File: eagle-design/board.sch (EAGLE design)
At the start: 13 parts, among them IC1 7805T

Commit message: Addedd new design
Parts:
- removed JP6: (no value), pinhead:PINHD-1X4
- added JP9: (no value), pinhead:PINHD-1X10
- added R2, R3, R4, R5, R6, R7, R8, R9: 10k, rcl:R-US_0207/10
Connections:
- new net N$13: B1.33, JP1.14
- new net N$14: B1.3, U$1.D0
- new net N$15: JP1.11, U$1.D2
- new net N$16: B1.29, JP1.12
- new net N$17: B1.31, JP1.13
- new net N$18: B1.35, JP1.15
- new net N$19: JP1.16, U$1.D1
- new net N$20: JP1.6, U$1.D6
- new net N$21: JP1.3, U$1.D8
- new net N$22: JP1.4, U$1.D5
- new net N$23: B1.53/!CS, JP1.7
- new net N$24: JP1.5, U$1.D7
- new net N$25: B1.52/SCK, JP1.8
- new net N$26: B1.51/MOSI, JP1.9
- new net N$27: B1.25, JP9.3, R2.2
- new net N$28: B1.50/MISO, JP1.10
- new net N$29: B1.27, JP9.4, R3.1
- new net N$30: B1.37, JP9.5, R4.1
- new net N$31: B1.39, JP9.6, R5.1
- new net N$32: B1.41, JP9.7, R6.1
- new net N$33: B1.43, JP9.8, R7.1
- new net N$34: B1.45, JP9.9, R8.1
- new net N$35: B1.47, JP9.10, R9.1
- new net N$9: B1.2, U$1.D4
- net N$11: no longer JP6.4
- net N$2: now also JP1.2
- net N$3: now also JP9.1, R2.1, R3.2, R4.2, R5.2, R6.2, R7.2, R8.2, R9.2; no longer JP6.1
- net N$4: now also JP1.1
- net N$5: now also B1.23
- net N$6: no longer JP6.3
- net N$7: now also JP9.2; no longer JP6.2
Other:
- moved on the sheet: IC1, J2, JP2, JP3, JP4, JP5, JP7, JP8, R1, U$1

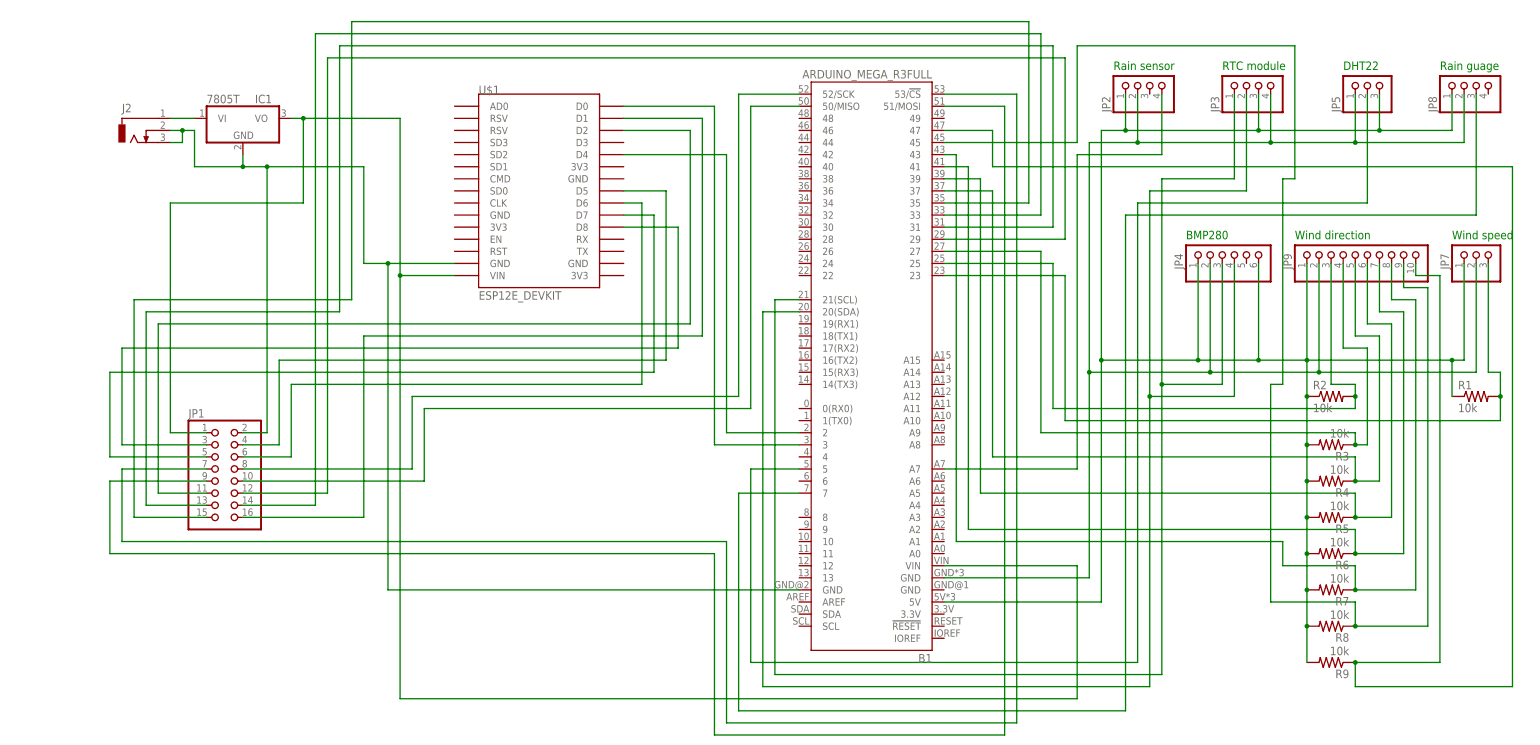
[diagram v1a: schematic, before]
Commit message: Added motherboard design and image exports
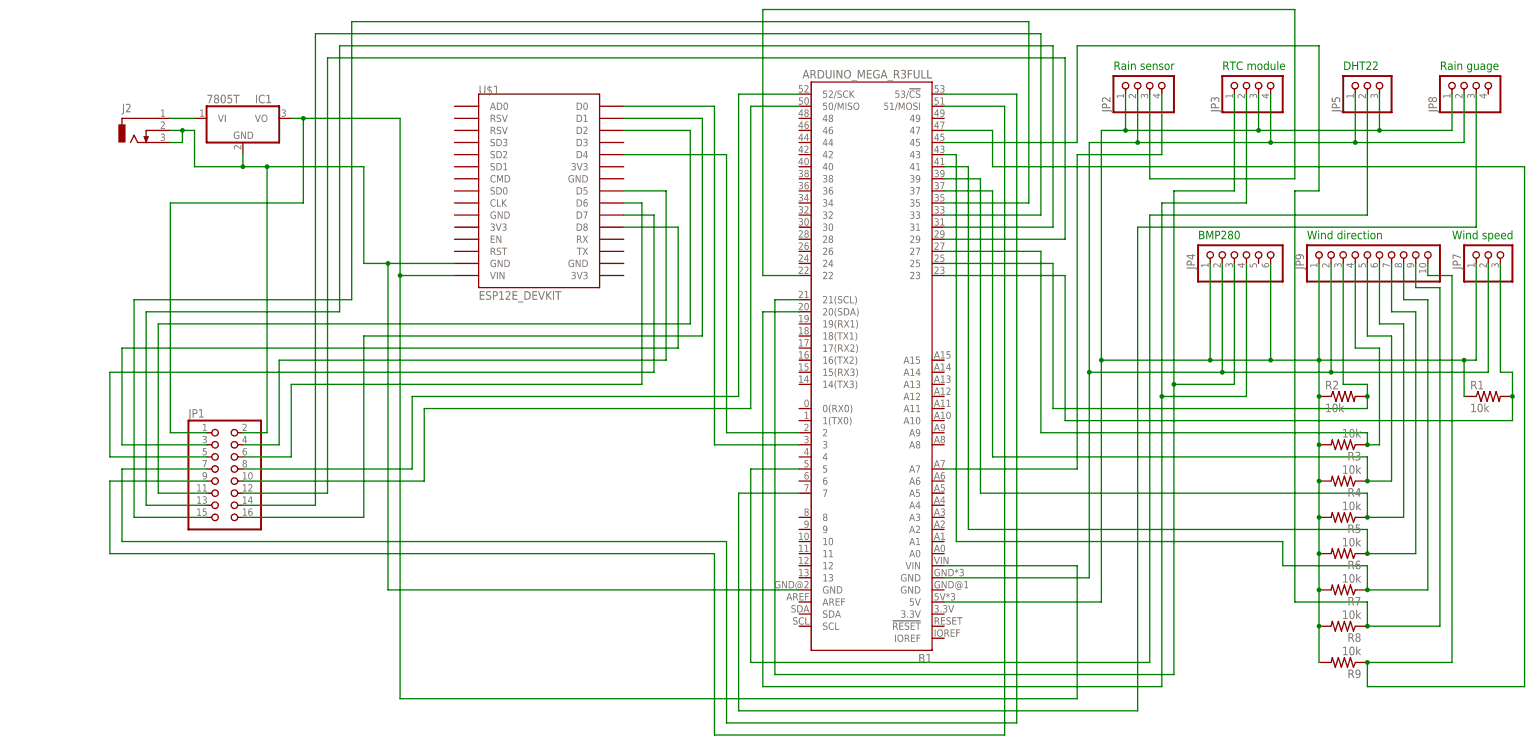
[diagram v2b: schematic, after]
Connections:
- new net N$36: B1.22, JP2.3
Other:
- moved on the sheet: JP4, JP7, JP9, R1, R2, R3, R4, R5, R6, R7, R8, R9

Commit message: Added new design
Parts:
- added R10, R11: 10k, rcl:R-US_0207/10
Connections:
- removed net N$11: B1.20(SDA), JP3.2, JP4.4
- removed net N$6: B1.21(SCL), JP3.1, JP4.3
- new net N$91: B1.21(SCL), JP3.1, JP4.3, R10.1
- new net N$92: B1.20(SDA), JP3.2, JP4.4, R11.1
- net N$3: now also R10.2, R11.2
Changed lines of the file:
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@@
 <part name="R8" library="rcl" library_urn="urn:adsk.eagle:library:334" deviceset="R-US_" device="0207/10" package3d_urn="urn:adsk.eagle:package:23491/2" value="10k"/>
 <part name="R9" library="rcl" library_urn="urn:adsk.eagle:library:334" deviceset="R-US_" device="0207/10" package3d_urn="urn:adsk.eagle:package:23491/2" value="10k"/>
+<part name="R10" library="rcl" library_urn="urn:adsk.eagle:library:334" deviceset="R-US_" device="0207/10" package3d_urn="urn:adsk.eagle:package:23491/2" value="10k"/>
+<part name="R11" library="rcl" library_urn="urn:adsk.eagle:library:334" deviceset="R-US_" device="0207/10" package3d_urn="urn:adsk.eagle:package:23491/2" value="10k"/>
 </parts>
 <sheets>
@@
 <attribute name="NAME" x="295.91" y="18.8214" size="1.778" layer="95" rot="R180"/>
 <attribute name="VALUE" x="295.91" y="23.622" size="1.778" layer="96" rot="R180"/>
+</instance>
+<instance part="R10" gate="G$1" x="266.7" y="38.1" smashed="yes" rot="R180">
+<attribute name="NAME" x="270.51" y="36.6014" size="1.778" layer="95" rot="R180"/>
+<attribute name="VALUE" x="270.51" y="41.402" size="1.778" layer="96" rot="R180"/>
+</instance>
+<instance part="R11" gate="G$1" x="266.7" y="30.48" smashed="yes" rot="R180">
+<attribute name="NAME" x="270.51" y="28.9814" size="1.778" layer="95" rot="R180"/>
+<attribute name="VALUE" x="270.51" y="33.782" size="1.778" layer="96" rot="R180"/>
 </instance>
 </instances>
@@
 <pinref part="R9" gate="G$1" pin="2"/>
 <wire x1="287.02" y1="27.94" x2="287.02" y2="20.32" width="0.1524" layer="91"/>
+<wire x1="241.3" y1="33.02" x2="259.08" y2="33.02" width="0.1524" layer="91"/>
+<junction x="241.3" y="33.02"/>
+<wire x1="259.08" y1="33.02" x2="259.08" y2="38.1" width="0.1524" layer="91"/>
+<pinref part="R10" gate="G$1" pin="2"/>
+<wire x1="259.08" y1="38.1" x2="261.62" y2="38.1" width="0.1524" layer="91"/>
+<wire x1="259.08" y1="33.02" x2="259.08" y2="30.48" width="0.1524" layer="91"/>
+<junction x="259.08" y="33.02"/>
+<pinref part="R11" gate="G$1" pin="2"/>
+<wire x1="259.08" y1="30.48" x2="261.62" y2="30.48" width="0.1524" layer="91"/>
 </segment>
 </net>
@@
 </segment>
 </net>
-<net name="N$6" class="0">
-<segment>
-<pinref part="JP3" gate="A" pin="1"/>
-<wire x1="269.24" y1="139.7" x2="269.24" y2="119.38" width="0.1524" layer="91"/>
-<wire x1="269.24" y1="119.38" x2="256.54" y2="119.38" width="0.1524" layer="91"/>
-<pinref part="JP4" gate="A" pin="3"/>
-<wire x1="269.24" y1="104.14" x2="269.24" y2="78.74" width="0.1524" layer="91"/>
-<wire x1="269.24" y1="78.74" x2="256.54" y2="78.74" width="0.1524" layer="91"/>
-<wire x1="256.54" y1="78.74" x2="256.54" y2="119.38" width="0.1524" layer="91"/>
-<junction x="256.54" y="78.74"/>
-<wire x1="256.54" y1="78.74" x2="256.54" y2="17.78" width="0.1524" layer="91"/>
-<pinref part="B1" gate="B1" pin="21(SCL)"/>
-<wire x1="177.8" y1="96.52" x2="172.72" y2="96.52" width="0.1524" layer="91"/>
-<wire x1="172.72" y1="96.52" x2="172.72" y2="17.78" width="0.1524" layer="91"/>
-<wire x1="172.72" y1="17.78" x2="256.54" y2="17.78" width="0.1524" layer="91"/>
-</segment>
-</net>
-<net name="N$11" class="0">
-<segment>
-<pinref part="JP3" gate="A" pin="2"/>
-<wire x1="271.78" y1="139.7" x2="271.78" y2="116.84" width="0.1524" layer="91"/>
-<wire x1="271.78" y1="116.84" x2="254" y2="116.84" width="0.1524" layer="91"/>
-<wire x1="254" y1="116.84" x2="254" y2="76.2" width="0.1524" layer="91"/>
-<pinref part="JP4" gate="A" pin="4"/>
-<wire x1="271.78" y1="104.14" x2="271.78" y2="76.2" width="0.1524" layer="91"/>
-<wire x1="271.78" y1="76.2" x2="254" y2="76.2" width="0.1524" layer="91"/>
-<junction x="254" y="76.2"/>
-<pinref part="B1" gate="B1" pin="20(SDA)"/>
-<wire x1="177.8" y1="93.98" x2="170.18" y2="93.98" width="0.1524" layer="91"/>
-<wire x1="170.18" y1="93.98" x2="170.18" y2="15.24" width="0.1524" layer="91"/>
-<wire x1="170.18" y1="15.24" x2="254" y2="15.24" width="0.1524" layer="91"/>
-<wire x1="254" y1="15.24" x2="254" y2="76.2" width="0.1524" layer="91"/>
-</segment>
-</net>
 <net name="N$10" class="0">
 <segment>
@@
 </segment>
 </net>
+<net name="N$91" class="0">
+<segment>
+<pinref part="R10" gate="G$1" pin="1"/>
+<wire x1="274.32" y1="38.1" x2="271.78" y2="38.1" width="0.1524" layer="91"/>
+<wire x1="274.32" y1="38.1" x2="274.32" y2="43.18" width="0.1524" layer="91"/>
+<pinref part="JP3" gate="A" pin="1"/>
+<wire x1="269.24" y1="139.7" x2="269.24" y2="119.38" width="0.1524" layer="91"/>
+<wire x1="269.24" y1="119.38" x2="256.54" y2="119.38" width="0.1524" layer="91"/>
+<pinref part="JP4" gate="A" pin="3"/>
+<wire x1="269.24" y1="104.14" x2="269.24" y2="78.74" width="0.1524" layer="91"/>
+<wire x1="269.24" y1="78.74" x2="256.54" y2="78.74" width="0.1524" layer="91"/>
+<wire x1="256.54" y1="78.74" x2="256.54" y2="119.38" width="0.1524" layer="91"/>
+<junction x="256.54" y="78.74"/>
+<wire x1="256.54" y1="78.74" x2="256.54" y2="43.18" width="0.1524" layer="91"/>
+<pinref part="B1" gate="B1" pin="21(SCL)"/>
+<wire x1="256.54" y1="43.18" x2="256.54" y2="17.78" width="0.1524" layer="91"/>
+<wire x1="177.8" y1="96.52" x2="172.72" y2="96.52" width="0.1524" layer="91"/>
+<wire x1="172.72" y1="96.52" x2="172.72" y2="17.78" width="0.1524" layer="91"/>
+<wire x1="172.72" y1="17.78" x2="256.54" y2="17.78" width="0.1524" layer="91"/>
+<wire x1="274.32" y1="43.18" x2="256.54" y2="43.18" width="0.1524" layer="91"/>
+<junction x="256.54" y="43.18"/>
+</segment>
+</net>
+<net name="N$92" class="0">
+<segment>
+<pinref part="R11" gate="G$1" pin="1"/>
+<wire x1="271.78" y1="30.48" x2="274.32" y2="30.48" width="0.1524" layer="91"/>
+<wire x1="274.32" y1="30.48" x2="274.32" y2="25.4" width="0.1524" layer="91"/>
+<pinref part="JP3" gate="A" pin="2"/>
+<wire x1="271.78" y1="139.7" x2="271.78" y2="116.84" width="0.1524" layer="91"/>
+<wire x1="271.78" y1="116.84" x2="254" y2="116.84" width="0.1524" layer="91"/>
+<wire x1="254" y1="116.84" x2="254" y2="76.2" width="0.1524" layer="91"/>
+<pinref part="JP4" gate="A" pin="4"/>
+<wire x1="271.78" y1="104.14" x2="271.78" y2="76.2" width="0.1524" layer="91"/>
+<wire x1="271.78" y1="76.2" x2="254" y2="76.2" width="0.1524" layer="91"/>
+<junction x="254" y="76.2"/>
+<pinref part="B1" gate="B1" pin="20(SDA)"/>
+<wire x1="177.8" y1="93.98" x2="170.18" y2="93.98" width="0.1524" layer="91"/>
+<wire x1="170.18" y1="93.98" x2="170.18" y2="15.24" width="0.1524" layer="91"/>
+<wire x1="170.18" y1="15.24" x2="254" y2="15.24" width="0.1524" layer="91"/>
+<wire x1="254" y1="15.24" x2="254" y2="25.4" width="0.1524" layer="91"/>
+<wire x1="254" y1="25.4" x2="254" y2="76.2" width="0.1524" layer="91"/>
+<wire x1="274.32" y1="25.4" x2="254" y2="25.4" width="0.1524" layer="91"/>
+<junction x="254" y="25.4"/>
+</segment>
+</net>

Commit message: Updated eagle design
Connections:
- net N$14: now also U$1.D3; no longer U$1.D0
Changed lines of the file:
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@@
 <pinref part="B1" gate="B1" pin="2"/>
 <wire x1="177.8" y1="68.58" x2="162.56" y2="68.58" width="0.1524" layer="91"/>
+<wire x1="162.56" y1="127" x2="162.56" y2="68.58" width="0.1524" layer="91"/>
 <pinref part="U$1" gate="G$1" pin="D4"/>
 <wire x1="140.97" y1="127" x2="162.56" y2="127" width="0.1524" layer="91"/>
-<wire x1="162.56" y1="127" x2="162.56" y2="68.58" width="0.1524" layer="91"/>
 </segment>
 </net>
 <net name="N$14" class="0">
 <segment>
-<pinref part="U$1" gate="G$1" pin="D0"/>
-<wire x1="140.97" y1="137.16" x2="160.02" y2="137.16" width="0.1524" layer="91"/>
-<wire x1="160.02" y1="137.16" x2="160.02" y2="66.04" width="0.1524" layer="91"/>
 <pinref part="B1" gate="B1" pin="3"/>
+<wire x1="160.02" y1="129.54" x2="160.02" y2="66.04" width="0.1524" layer="91"/>
 <wire x1="160.02" y1="66.04" x2="177.8" y2="66.04" width="0.1524" layer="91"/>
+<pinref part="U$1" gate="G$1" pin="D3"/>
+<wire x1="140.97" y1="129.54" x2="160.02" y2="129.54" width="0.1524" layer="91"/>
 </segment>
 </net>
